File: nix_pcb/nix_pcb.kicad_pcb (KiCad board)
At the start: 2 copper layers, 163.5 x 60 mm, 76 parts, among them IC1 DS3234SN#, J1 Barrel_Jack, J2 Conn_01x05, J3 Conn_01x05, J4 Conn_01x06, J5 Conn_ARM_JTAG_SWD_10, J6 Conn_01x06, Q1 MMBTA92, Q2 MMBTA92, Q3 MMBTA92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

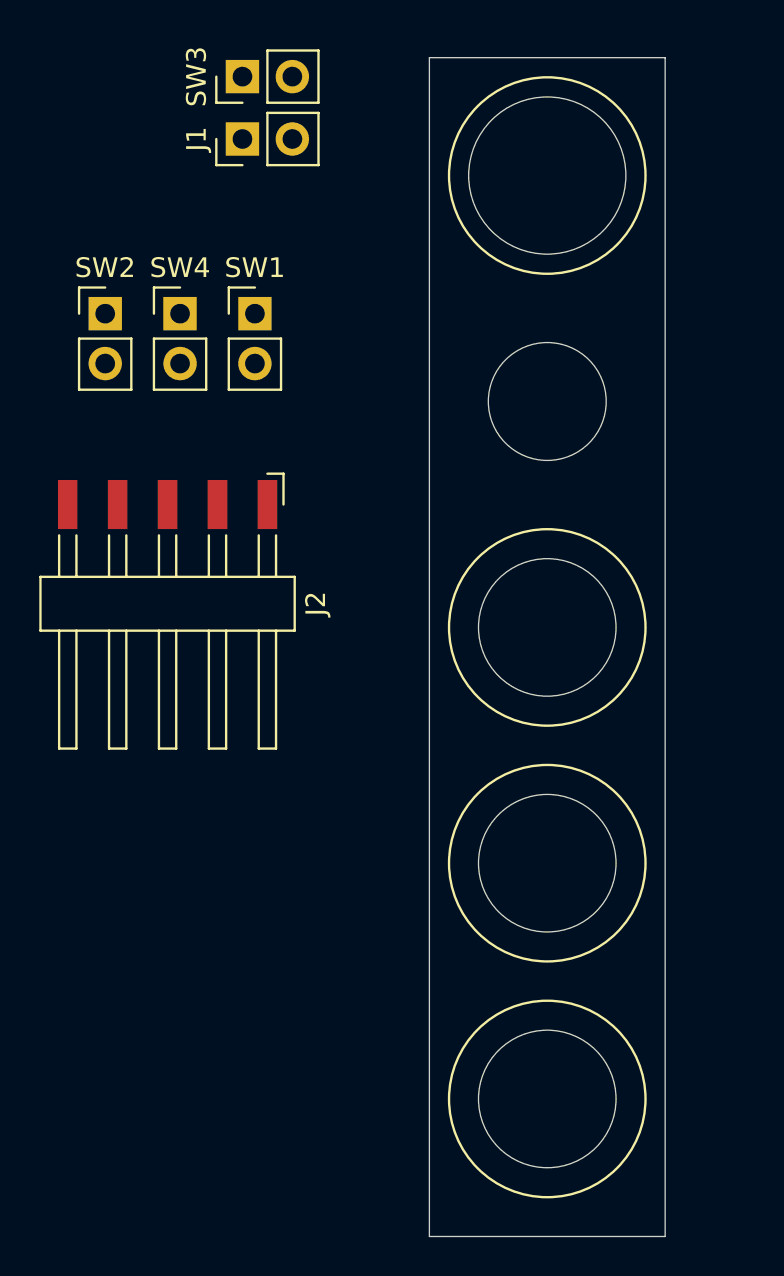
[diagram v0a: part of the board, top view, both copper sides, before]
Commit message: removed button board
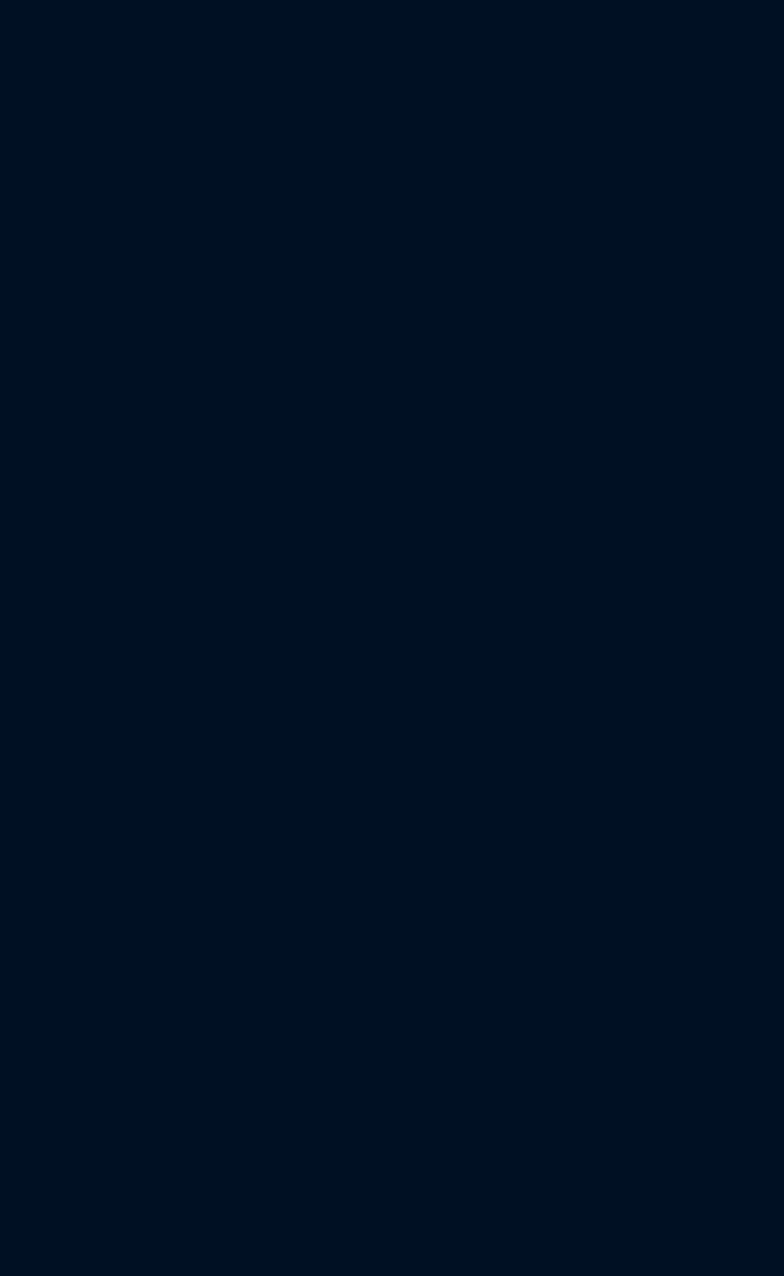
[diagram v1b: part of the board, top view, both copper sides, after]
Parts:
- removed J1: Barrel_Jack, Connector_PinHeader_2.54mm:PinHeader_1x02_P2.54mm_Vertical
- removed J2: Conn_01x05, Connector_Harwin:Harwin_M20-89005xx_1x05_P2.54mm_Horizontal
- removed SW1, SW2, SW4: SW_Push, Connector_PinHeader_2.54mm:PinHeader_1x02_P2.54mm_Vertical
- removed SW3: SW_SPDT, Connector_PinHeader_2.54mm:PinHeader_1x02_P2.54mm_Vertical
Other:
- board size 163.5 x 60 mm -> 143.5 x 60 mm

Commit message: add gnd to ext-conn and add silkscreen text to connectors
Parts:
- removed J6: Conn_01x06, Connector_Harwin:Harwin_M20-89006xx_1x06_P2.54mm_Horizontal
- added J1: Conn_01x07, Connector_Harwin:Harwin_M20-89007xx_1x07_P2.54mm_Horizontal, F.Cu at (181.6, 109.2)
- moved D5 12.1 mm to (193.0, 105.4), turned to 90 degrees
- moved C5 7.62 mm to (201.9, 104.1)
- moved U2 7.62 mm to (207.4, 105.2)
- moved C4 7.62 mm to (199.4, 106.0)
- moved R3 7.24 mm to (196.2, 105.4)
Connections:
- D5 pad 2: /controller/Ext0 -> /controller/Ext4
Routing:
- net GND: track 144.2 -> 164.0 mm, vias 39 -> 49
- net /controller/Ext4: track 60.0 -> 70.4 mm
- net /controller/Ext0: track 83.4 -> 73.7 mm, vias 3 -> 2
- net +5V: track 237.2 -> 246.4 mm
- net Net-(D5-Pad1): track 2.51 -> 3.39 mm
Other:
- board text added: "+12 V"
- board text added: "+3V3"
- board text added: "+5 V"
- board text added: "DOWN"
- board text added: "EXT0"
- board text added: "EXT1"
- board text added: "EXT2"
- board text added: "EXT3"
- board text added: "EXT4"
- board text added: "GND"
- board text added: "SET"
- board text added: "UP"
- board text added: "VAA (~~140 V)"
- board text added: "VPP"
